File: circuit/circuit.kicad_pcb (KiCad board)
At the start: 2 copper layers, 30 x 40 mm, 30 parts, among them J1 JST-PH_2_RA, U1 SK812, U2 LM1117MPX-3.3, U3 ADXL345, U4 ATmega328-AU, U5 USB_MicroB, Y1 Crystal_SMD

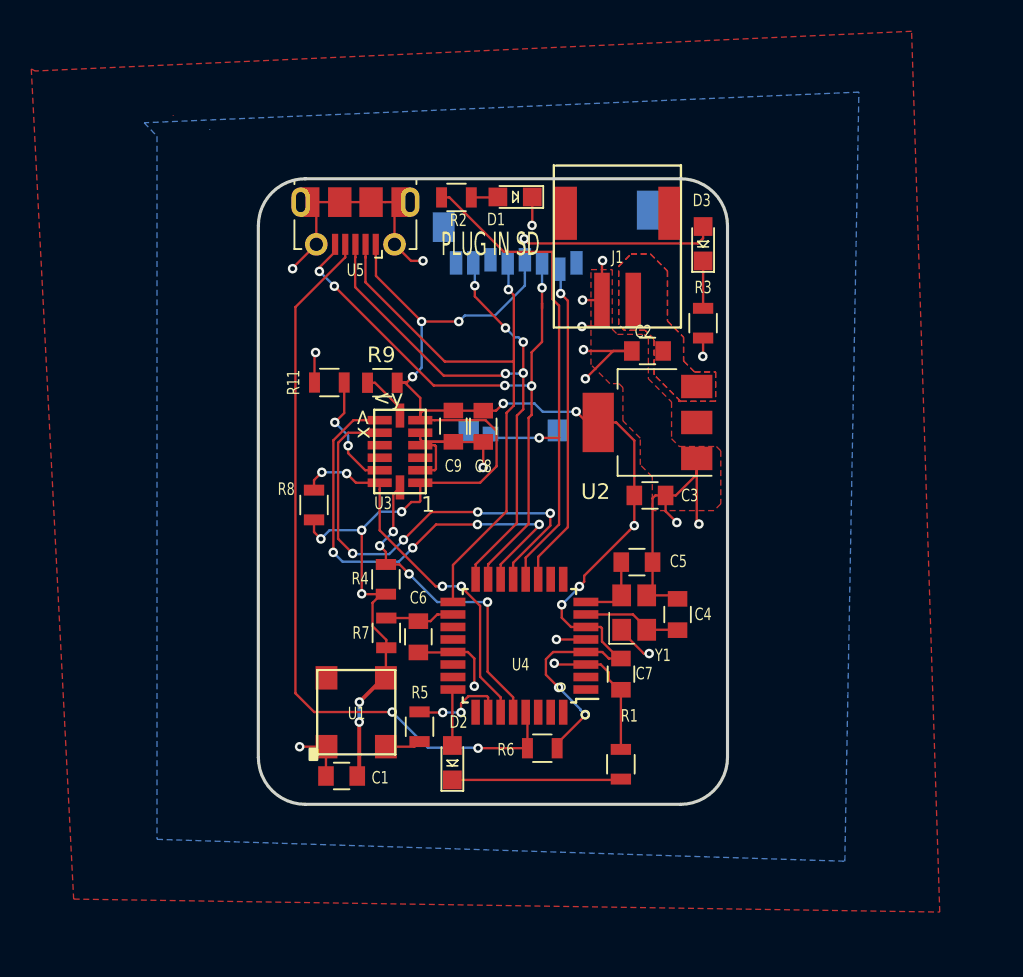
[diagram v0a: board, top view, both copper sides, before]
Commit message: Layout with a 2x03 connector
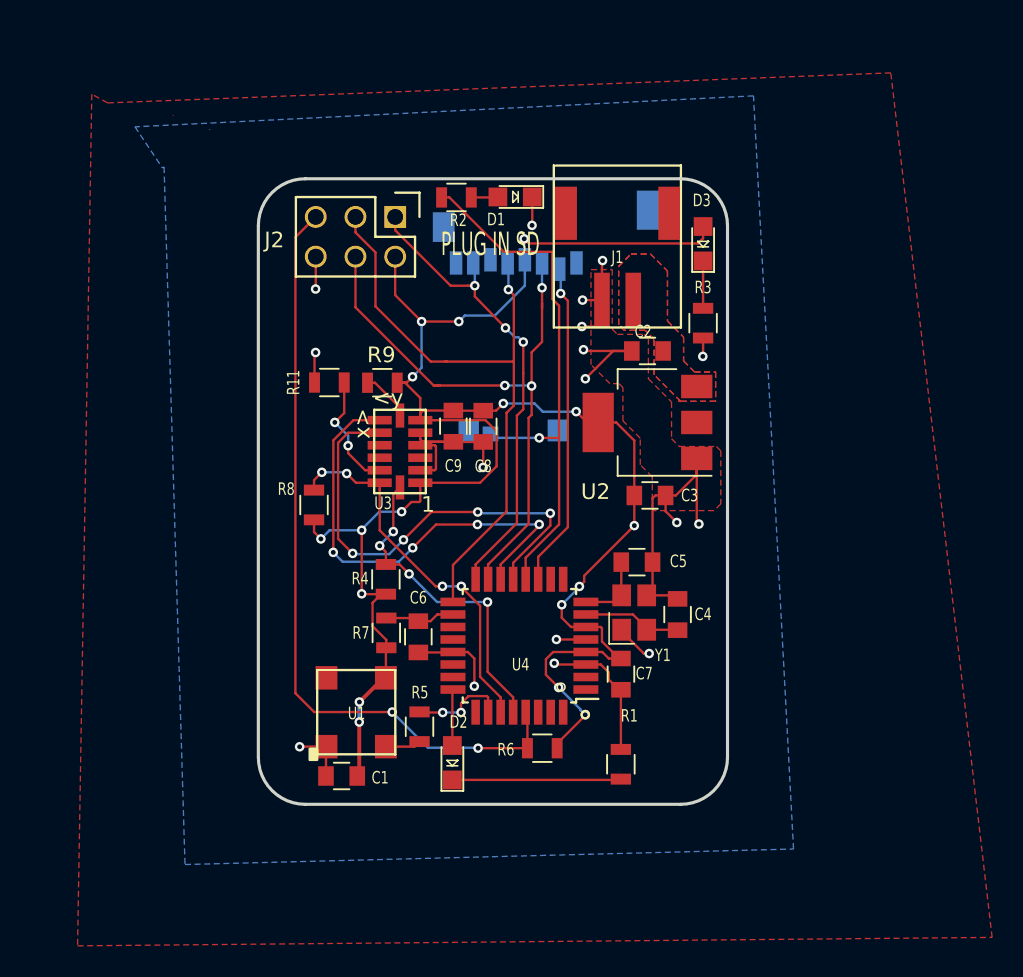
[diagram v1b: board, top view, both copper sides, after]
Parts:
- removed U5: USB_MicroB, Connectors_USB:USB_Micro-B_Molex-105017-0001
- added J2: CONN_02X03, footprints:Pin_Header_Straight_2x03, F.Cu at (191.9, 77.0)
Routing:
- net GND: track 90.0 -> 74.7 mm, vias 18 -> 17
- net /MISO: track 38.9 -> 30.4 mm, vias 5 -> 3
- net /SCK: track 37.5 -> 40.1 mm
- net /MOSI: track 40.7 -> 39.0 mm, vias 5 -> 3
- net VCC: track 125.7 -> 124.4 mm
- net /RESET: track 48.7 -> 49.6 mm
- added copper zone on F.Cu, net VCC

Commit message: Fixed the text labels and revision number.
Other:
- board text added: "REV - 5 - 2019"
- board text removed: "REV - 3 - 2019"
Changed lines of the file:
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@@
   (module rocketry:Micro_SD_Card_Holder_Molex (layer B.Cu)
     (at 196.596 90.678)
-    (fp_text reference SD1 (at -0.49 6.598) (layer B.SilkS)
+    (fp_text reference SD1 (at 5.358 1.618) (layer B.SilkS)
       (effects (font (size 1 1) (thickness 0.15)) (justify mirror))
     )
@@
     (tags "QFP 0.8")
     (attr smd)
-    (fp_text reference U4 (at -0.0762 -1.20396 180) (layer F.SilkS)
+    (fp_text reference U4 (at -0.01708 6.33072 180) (layer F.SilkS)
       (effects (font (size 0.8 0.6) (thickness 0.125)))
     )
@@
     (fp_circle (center -2.667 -2.6416) (end -2.667 -2.6924) (layer F.SilkS) (width 0.5))
     (fp_circle (center -4.2164 -4.3942) (end -4.2164 -4.445) (layer F.SilkS) (width 0.5))
-    (fp_text user %R (at 0 0 180) (layer F.Fab)
+    (fp_text user %R (at 0.06292 -1.43928 180) (layer F.Fab) hide
       (effects (font (size 1 1) (thickness 0.15)))
     )
@@
     (tags "capacitor 0805")
     (attr smd)
-    (fp_text reference C2 (at 0.272 1.242 180) (layer F.SilkS)
+    (fp_text reference C2 (at 2.632 0.002 180) (layer F.SilkS)
       (effects (font (size 0.8 0.6) (thickness 0.125)))
     )
@@
     (tags "CMS SOT")
     (attr smd)
-    (fp_text reference U2 (at 3.322 -4.426 180) (layer F.SilkS)
+    (fp_text reference U2 (at 5.542 -0.006 180) (layer F.SilkS)
       (effects (font (size 1 1) (thickness 0.15)))
     )
@@
   (module rocketry:ADXL345 (layer F.Cu)
     (at 192.2 92.025 180)
-    (fp_text reference U3 (at 1.08 -3.31 180) (layer F.SilkS)
+    (fp_text reference U3 (at 0.036 -4.061 180) (layer F.SilkS)
       (effects (font (size 0.8 0.6) (thickness 0.125)))
     )
@@
       (effects (font (size 0.8 0.6) (thickness 0.125)))
     )
-    (fp_text user <y (at 0.762 3.429 180) (layer F.SilkS)
+    (fp_text user <y (at -1.444 3.479 180) (layer F.SilkS)
       (effects (font (size 1 1) (thickness 0.15)))
     )
-    (fp_text user x> (at 2.413 1.778 270) (layer F.SilkS)
+    (fp_text user x> (at 3.076 1.369 270) (layer F.SilkS)
       (effects (font (size 1 1) (thickness 0.15)))
     )
-    (fp_text user 1 (at -1.7907 -3.3909 180) (layer F.SilkS)
+    (fp_text user 1 (at -2.594 -3.231 180) (layer F.SilkS)
       (effects (font (size 1 1) (thickness 0.125)))
     )
@@
     (tags "resistor 0805")
     (attr smd)
-    (fp_text reference R11 (at 2.29 0 270) (layer F.SilkS)
+    (fp_text reference R11 (at -0.02 1.66) (layer F.SilkS)
       (effects (font (size 0.8 0.6) (thickness 0.125)))
     )
@@
     (tags "resistor 0805")
     (attr smd)
-    (fp_text reference R2 (at 0.12 1.46) (layer F.SilkS)
+    (fp_text reference R2 (at -0.016 1.546) (layer F.SilkS)
       (effects (font (size 0.8 0.6) (thickness 0.125)))
     )
@@
     (tags "capacitor 0805")
     (attr smd)
-    (fp_text reference C1 (at -2.466 -0.11) (layer F.SilkS)
+    (fp_text reference C1 (at -2.466 -0.02) (layer F.SilkS)
       (effects (font (size 0.8 0.6) (thickness 0.125)))
     )
@@
     (tags "capacitor 0805")
     (attr smd)
-    (fp_text reference C4 (at 0.0127 1.63576 180) (layer F.SilkS)
+    (fp_text reference C4 (at 2.414 0.014 180) (layer F.SilkS)
       (effects (font (size 0.8 0.6) (thickness 0.125)))
     )
@@
     (tags "capacitor 0805")
     (attr smd)
-    (fp_text reference C5 (at 2.654 -0.05402) (layer F.SilkS)
+    (fp_text reference C5 (at 0.024 -1.50402) (layer F.SilkS)
       (effects (font (size 0.8 0.6) (thickness 0.125)))
     )
@@
     (tags "capacitor 0805")
     (attr smd)
-    (fp_text reference C6 (at -2.5 0) (layer F.SilkS)
+    (fp_text reference C6 (at -2.509 0.011) (layer F.SilkS)
       (effects (font (size 0.8 0.6) (thickness 0.125)))
     )
@@
     (tags "capacitor 0805")
     (attr smd)
-    (fp_text reference C7 (at 0.0381 1.49352 180) (layer F.SilkS)
+    (fp_text reference C7 (at -0.03394 1.54484 180) (layer F.SilkS)
       (effects (font (size 0.8 0.6) (thickness 0.125)))
     )
@@
     (tags "LED led 0805 SMD smd SMT smt smdled SMDLED smtled SMTLED")
     (attr smd)
-    (fp_text reference D1 (at 1.22 -1.44 180) (layer F.SilkS)
+    (fp_text reference D1 (at 0.066 -1.476 180) (layer F.SilkS)
       (effects (font (size 0.8 0.6) (thickness 0.125)))
     )
@@
     (tags "LED led 0805 SMD smd SMT smt smdled SMDLED smtled SMTLED")
     (attr smd)
-    (fp_text reference D2 (at 2.60096 0.39116 180) (layer F.SilkS)
+    (fp_text reference D2 (at 0.019 1.694 180) (layer F.SilkS)
       (effects (font (size 0.8 0.6) (thickness 0.125)))
     )
@@
     (tags "LED led 0805 SMD smd SMT smt smdled SMDLED smtled SMTLED")
     (attr smd)
-    (fp_text reference D3 (at 2.7715 -0.08866 -180) (layer F.SilkS)
+    (fp_text reference D3 (at 2.684 -0.188 -180) (layer F.SilkS)
       (effects (font (size 0.8 0.6) (thickness 0.125)))
     )
@@
     (tags "resistor 0805")
     (attr smd)
-    (fp_text reference R1 (at -3.09804 -0.53982) (layer F.SilkS)
+    (fp_text reference R1 (at -2.109 -0.039) (layer F.SilkS)
       (effects (font (size 0.8 0.6) (thickness 0.125)))
     )
@@
     (tags "resistor 0805")
     (attr smd)
-    (fp_text reference R7 (at -0.001 -1.621 -180) (layer F.SilkS)
+    (fp_text reference R7 (at -0.021 -1.661 -180) (layer F.SilkS)
       (effects (font (size 0.8 0.6) (thickness 0.125)))
     )
@@
   (module rocketry:SK6812 (layer F.Cu)
     (at 191.3 108.7 270)
-    (fp_text reference U1 (at 0.075 1.875 180) (layer F.SilkS)
+    (fp_text reference U1 (at -3.514 1.956 180) (layer F.SilkS)
       (effects (font (size 0.8 0.6) (thickness 0.125)))
     )
@@
     (tags "SMD SMT crystal hand-soldering")
     (attr smd)
-    (fp_text reference Y1 (at -2.7318 1.8363 180) (layer F.SilkS)
+    (fp_text reference Y1 (at -2.751 0.729 180) (layer F.SilkS)
       (effects (font (size 0.8 0.6) (thickness 0.125)))
     )
@@
     (tags "capacitor 0805")
     (attr smd)
-    (fp_text reference C3 (at 2.54 0 -180) (layer F.SilkS)
+    (fp_text reference C3 (at -2.58 0.1 -180) (layer F.SilkS)
       (effects (font (size 0.8 0.6) (thickness 0.125)))
     )
@@
     (tags "resistor 0805")
     (attr smd)
-    (fp_text reference R8 (at 1.016 -1.778 -180) (layer F.SilkS)
+    (fp_text reference R8 (at -0.02 1.86 -180) (layer F.SilkS)
       (effects (font (size 0.8 0.6) (thickness 0.125)))
     )
@@
     (tags "capacitor 0805")
     (attr smd)
-    (fp_text reference C8 (at 2.556 0) (layer F.SilkS)
+    (fp_text reference C8 (at 2.55 0.01) (layer F.SilkS)
       (effects (font (size 0.8 0.6) (thickness 0.125)))
     )
@@
     (tags "capacitor 0805")
     (attr smd)
-    (fp_text reference C9 (at 2.54 0) (layer F.SilkS)
+    (fp_text reference C9 (at 2.53 0.01) (layer F.SilkS)
       (effects (font (size 0.8 0.6) (thickness 0.125)))
     )
@@
     (tags "resistor 0805")
     (attr smd)
-    (fp_text reference R9 (at 0.066 1.778) (layer F.SilkS)
+    (fp_text reference R9 (at -0.02 1.734) (layer F.SilkS)
       (effects (font (size 1 1) (thickness 0.15)))
     )
@@
     (descr "Through hole pin header")
     (tags "pin header")
-    (fp_text reference J2 (at 1.48 7.73) (layer F.SilkS)
+    (fp_text reference J2 (at 5.24 2.62) (layer F.SilkS)
       (effects (font (size 1 1) (thickness 0.15)))
     )
@@
     )
   )
-  (gr_text "PLUG IN SD" (at 197.98 78.77) (layer F.SilkS)
+  (gr_text "PLUG IN SD" (at 198.094 80.046) (layer F.SilkS)
     (effects (font (size 1.5 0.8) (thickness 0.2)))
   )
-  (gr_text "REV - 3 - 2019" (at 197.684 112.636) (layer B.SilkS)
+  (gr_text "REV - 5 - 2019" (at 197.654 112.626) (layer B.SilkS)
     (effects (font (size 1.5 1.5) (thickness 0.3)) (justify mirror))
   )
-  (gr_text "WF\nAB\nSB" (at 185.91 98.66) (layer B.SilkS)
-    (effects (font (size 1.5 1.5) (thickness 0.2)) (justify mirror))
+  (gr_text "WF\nAB\nSB" (at 186.424 104.616) (layer B.SilkS)
+    (effects (font (size 2.5 2.5) (thickness 0.2)) (justify mirror))
   )
   (gr_arc (start 210.1434 77.586754) (end 213.1434 77.586754) (angle -90) (layer Edge.Cuts) (width 0.2))

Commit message: Added the pigeon mark on the back
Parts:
- added G***: LOGO, footprints:pigeon, B.Cu at (198.3, 86.0)
